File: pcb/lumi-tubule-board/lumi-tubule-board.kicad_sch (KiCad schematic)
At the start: 72 parts, among them Q1 DMN1045UFR4, Q10 DMN1045UFR4, Q11 DMN1045UFR4, Q12 DMN1045UFR4, Q13 DMN1045UFR4, Q2 DMN1045UFR4, Q3 DMN1045UFR4, Q4 DMN1045UFR4, Q5 DMN1045UFR4, Q6 DMN1045UFR4, Q7 DMN1045UFR4, Q8 DMN1045UFR4, Q9 DMN1045UFR4, SW1 SWITCH_TACT_SMT4.6X2.8, SW2 SWITCH_TACT_SMT4.6X2.8, U1 SHTC3, U2 VREG_SOT23-5, U3 ESP32-S3-MINI-1, U4 LIS2Dx12, X1 USB_C

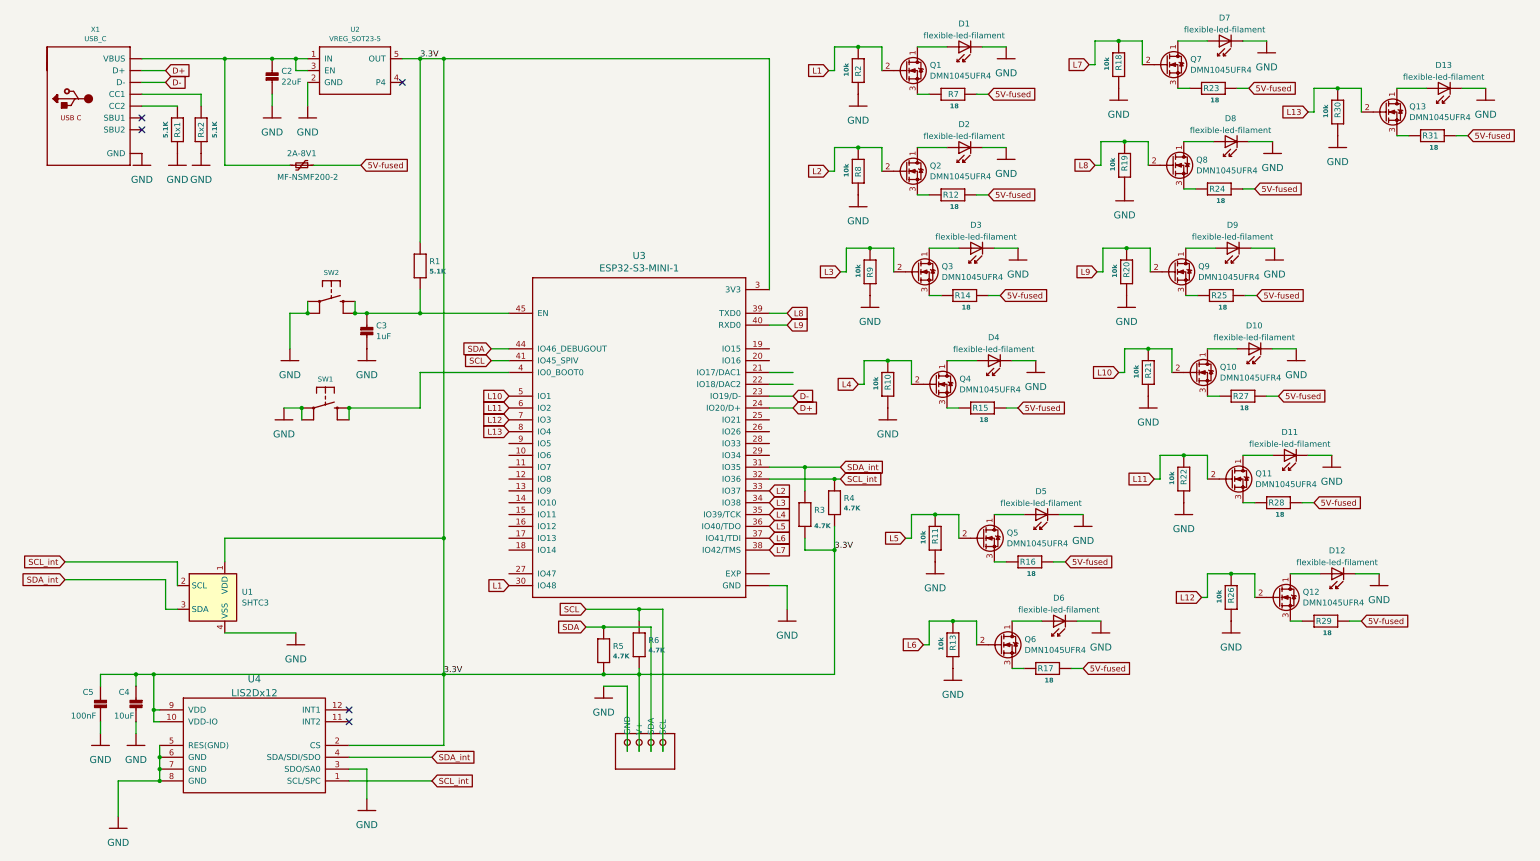
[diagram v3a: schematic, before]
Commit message: Add LED and fix pad numbers
Add low power LED to board and fix some missing links between schematic and pcb design.
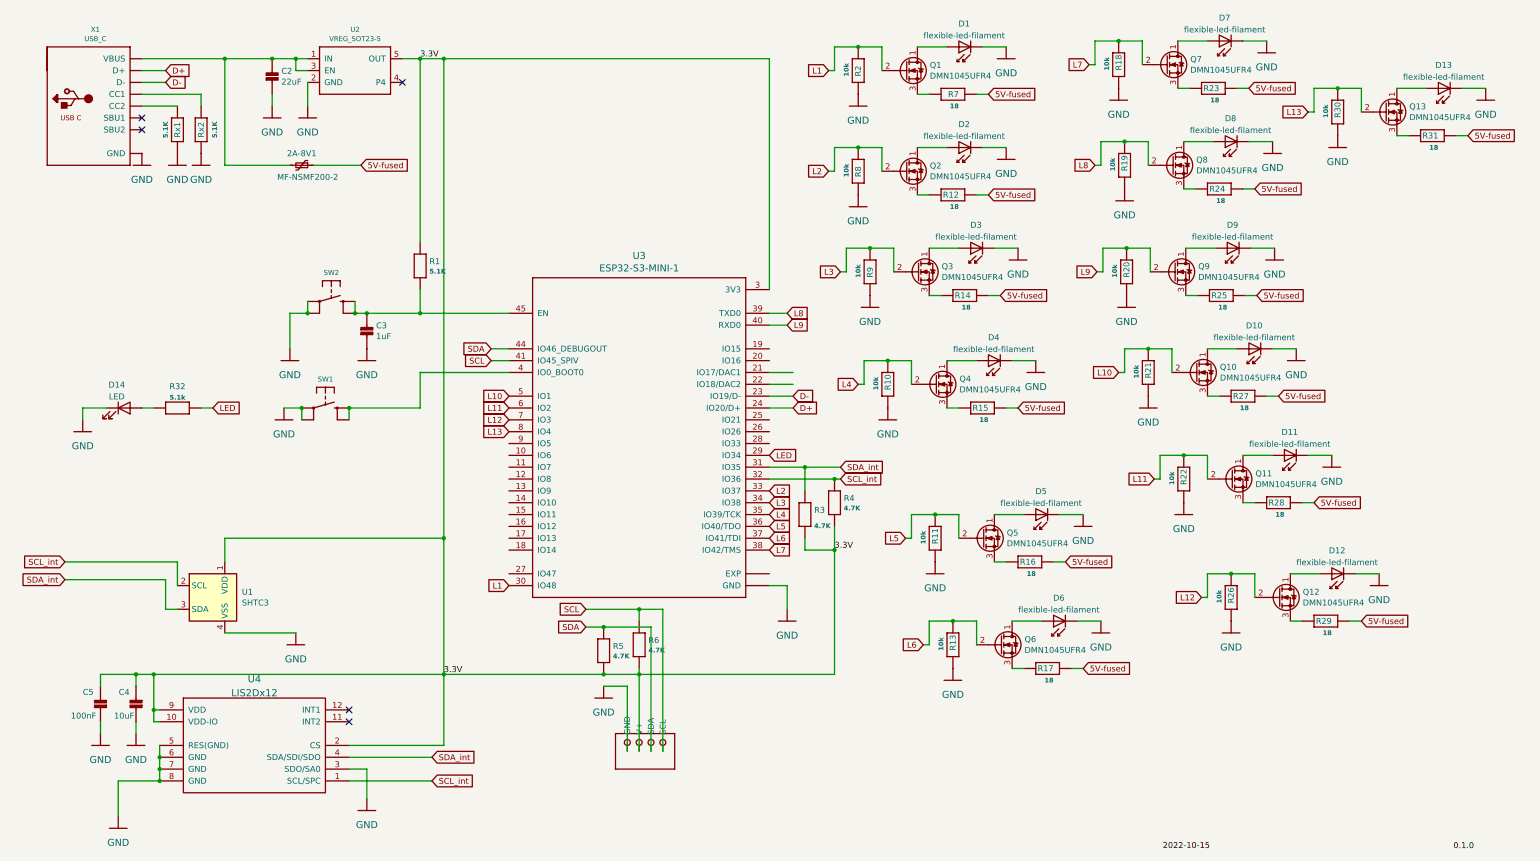
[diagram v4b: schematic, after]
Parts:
- added D14: LED, LED_SMD:LED_0603_1608Metric, symbol Device:LED
- added R32: 5.1k, Resistor_SMD:R_0603_1608Metric, symbol Adafruit_ESP32-S3_8MB_No_PSRAM-eagle-import:RESISTOR_0603
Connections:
- net GND: now also D14.1 (K)
- net LED: now reaches U3.29 (IO34)
- net LED: now also R32.2
- new net: D14.2 (A), R32.1
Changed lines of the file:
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@@
   (no_connect (at 85.09 166.37))
   (no_connect (at 96.52 29.21))
+  (wire (pts (xy 55.88 99.06) (xy 53.34 99.06))
+    (stroke (width 0) (type default) (color 0 0 0 0))
+  )
   (wire (pts (xy 44.45 171.45) (xy 44.45 173.99))
     (stroke (width 0) (type default) (color 0 0 0 0))
@@
     (stroke (width 0) (type default) (color 0 0 0 0))
   )
+  (wire (pts (xy 33.02 99.06) (xy 27.94 99.06))
+    (stroke (width 0) (type default) (color 0 0 0 0))
+  )
   (wire (pts (xy 209.55 149.86) (xy 208.28 149.86))
     (stroke (width 0) (type default) (color 0 0 0 0))
@@
     (stroke (width 0) (type default) (color 0 0 0 0))
   )
+  (wire (pts (xy 27.94 99.06) (xy 27.94 101.6))
+    (stroke (width 0) (type default) (color 0 0 0 0))
+  )
   (wire (pts (xy 195.58 93.98) (xy 194.31 93.98))
     (stroke (width 0) (type default) (color 0 0 0 0))
@@
     (stroke (width 0) (type default) (color 0 0 0 0))
   )
+  (wire (pts (xy 40.64 99.06) (xy 43.18 99.06))
+    (stroke (width 0) (type default) (color 0 0 0 0))
+  )
   (wire (pts (xy 287.02 134.62) (xy 293.37 134.62))
     (stroke (width 0) (type default) (color 0 0 0 0))
@@
     (stroke (width 0) (type default) (color 0 0 0 0))
   )
+  (label "0.1.0" (at 321.9947 193.9738 0)
+    (effects (font (size 1.27 1.27)) (justify left bottom))
+  )
   (label "3.3V" (at 100.33 24.13 0)
     (effects (font (size 1.27 1.27)) (justify left bottom))
@@
     (effects (font (size 1.27 1.27)) (justify left bottom))
   )
+  (label "2022-10-15" (at 259.6468 193.9551 0)
+    (effects (font (size 1.27 1.27)) (justify left bottom))
+  )
   (label "3.3V" (at 189.23 129.54 0)
     (effects (font (size 1.27 1.27)) (justify left bottom))
@@
     )
   )
+  (global_label "LED" (shape input) (at 175.26 109.22 0) (fields_autoplaced)
+    (effects (font (size 1.27 1.27)) (justify left))
+    (property "Intersheet References" "${INTERSHEET_REFS}" (id 0) (at 181.0313 109.1406 0)
+      (effects (font (size 1.27 1.27)) (justify left) hide)
+    )
+  )
   (global_label "5V-fused" (shape input) (at 228.6 99.06 0) (fields_autoplaced)
     (effects (font (size 1.27 1.27)) (justify left))
@@
     )
   )
+  (global_label "LED" (shape input) (at 55.88 99.06 0) (fields_autoplaced)
+    (effects (font (size 1.27 1.27)) (justify left))
+    (property "Intersheet References" "${INTERSHEET_REFS}" (id 0) (at 61.6513 98.9806 0)
+      (effects (font (size 1.27 1.27)) (justify left) hide)
+    )
+  )
   (global_label "L6" (shape input) (at 208.28 149.86 180) (fields_autoplaced)
     (effects (font (size 1.27 1.27)) (justify right))
@@
     (pin "2")
   )
+  (symbol (lib_id "Device:LED") (at 36.83 99.06 0) (unit 1)
+    (in_bom yes) (on_board yes) (fields_autoplaced)
+    (property "Reference" "D14" (id 0) (at 35.2425 94.0902 0))
+    (property "Value" "LED" (id 1) (at 35.2425 96.6271 0))
+    (property "Footprint" "LED_SMD:LED_0603_1608Metric" (id 2) (at 36.83 99.06 0)
+      (effects (font (size 1.27 1.27)) hide)
+    )
+    (property "Datasheet" "https://datasheet.lcsc.com/lcsc/1811101510_Everlight-Elec-19-217-GHC-YR1S2-3T_C72043.pdf" (id 3) (at 36.83 99.06 0)
+      (effects (font (size 1.27 1.27)) hide)
+    )
+    (property "JLCPCB ref" "C72043" (id 4) (at 36.83 99.06 0)
+      (effects (font (size 1.27 1.27)) hide)
+    )
+    (pin "1")
+    (pin "2")
+  )
   (symbol (lib_id "Adafruit_ESP32-S3_8MB_No_PSRAM-eagle-import:GND") (at 281.94 22.86 0) (unit 1)
     (in_bom yes) (on_board yes)
@@
     (pin "1")
   )
+  (symbol (lib_id "Adafruit_ESP32-S3_8MB_No_PSRAM-eagle-import:GND") (at 27.94 104.14 0) (unit 1)
+    (in_bom yes) (on_board yes)
+    (property "Reference" "#GND029" (id 0) (at 27.94 104.14 0)
+      (effects (font (size 1.27 1.27)) hide)
+    )
+    (property "Value" "GND" (id 1) (at 27.94 107.2134 0)
+      (effects (font (size 1.4986 1.4986)))
+    )
+    (property "Footprint" "" (id 2) (at 27.94 104.14 0)
+      (effects (font (size 1.27 1.27)) hide)
+    )
+    (property "Datasheet" "" (id 3) (at 27.94 104.14 0)
+      (effects (font (size 1.27 1.27)) hide)
+    )
+    (pin "1")
+  )
   (symbol (lib_id "Adafruit_ESP32-S3_8MB_No_PSRAM-eagle-import:GND") (at 297.18 43.18 0) (unit 1)
     (in_bom yes) (on_board yes)
@@
     (pin "1")
   )
+  (symbol (lib_id "Adafruit_ESP32-S3_8MB_No_PSRAM-eagle-import:RESISTOR_0603") (at 48.26 99.06 0) (unit 1)
+    (in_bom yes) (on_board yes) (fields_autoplaced)
+    (property "Reference" "R32" (id 0) (at 48.26 94.4294 0))
+    (property "Value" "5.1k" (id 1) (at 48.26 96.7952 0)
+      (effects (font (size 1.016 1.016) bold))
+    )
+    (property "Footprint" "Resistor_SMD:R_0603_1608Metric" (id 2) (at 48.26 99.06 0)
+      (effects (font (size 1.27 1.27)) hide)
+    )
+    (property "Datasheet" "https://datasheet.lcsc.com/lcsc/2206010130_UNI-ROYAL-Uniroyal-Elec-0603WAF2203T5E_C22961.pdf" (id 3) (at 48.26 99.06 0)
+      (effects (font (size 1.27 1.27)) hide)
+    )
+    (property "JLCPCB ref" "C22961" (id 4) (at 48.26 99.06 0)
+      (effects (font (size 1.27 1.27)) hide)
+    )
+    (pin "1")
+    (pin "2")
+  )
   (symbol (lib_id "Adafruit_ESP32-S3_8MB_No_PSRAM-eagle-import:RESISTOR_0603_NOOUT") (at 214.63 149.86 90) (unit 1)
     (in_bom yes) (on_board yes)
@@
       (reference "#GND028") (unit 1) (value "GND") (footprint "")
     )
+    (path "/503ce97c-80b8-42ab-a40d-e82c4bb84960"
+      (reference "#GND029") (unit 1) (value "GND") (footprint "")
+    )
     (path "/00000000-0000-0000-0000-000063154829"
       (reference "#GND0101") (unit 1) (value "GND") (footprint "")
@@
       (reference "D13") (unit 1) (value "flexible-led-filament") (footprint "lumi-tubule-board:Flexible LED filament viamount")
     )
+    (path "/053f1d49-9e2c-4c46-a418-1355f7c965dc"
+      (reference "D14") (unit 1) (value "LED") (footprint "LED_SMD:LED_0603_1608Metric")
+    )
     (path "/00000000-0000-0000-0000-00006318ab1b"
       (reference "Q1") (unit 1) (value "DMN1045UFR4") (footprint "lumi-tubule-board:DMN1045UFR4")
@@
       (reference "R31") (unit 1) (value "18") (footprint "Resistor_SMD:R_1206_3216Metric")
     )
+    (path "/dec5787c-6a1b-4721-bda6-97b2eff8c935"
+      (reference "R32") (unit 1) (value "5.1k") (footprint "Resistor_SMD:R_0603_1608Metric")
+    )
     (path "/00000000-0000-0000-0000-00006317c4f0"

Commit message: Fix MOSFET wiring
Fixed the MOSFETs' wiring, which was all wrong. Rerouted mosfet out via ground plane, freeing up space for the Vsup line on top of board. Removed the diagnosis LED line on the back of PCB which was interrupting ground plane flow. Swapped out the pulldown resistor for something smaller.
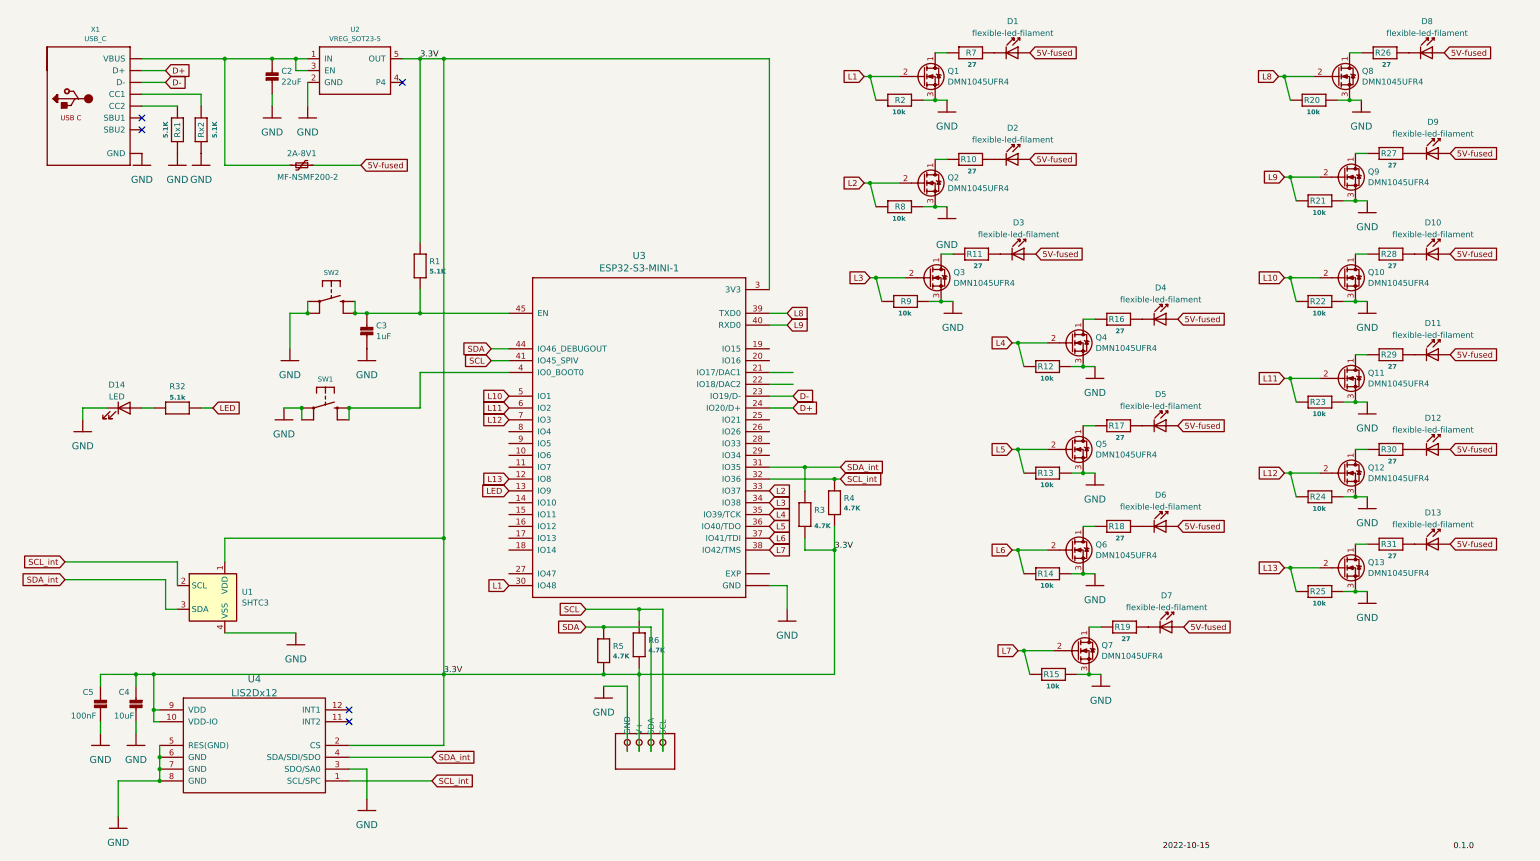
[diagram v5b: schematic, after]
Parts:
- Q1, Q10, Q11, Q12, Q13, Q2, Q3, Q4, Q5, Q6, Q7, Q8, Q9: JLCPCB ref (none) -> C460988
- R10, R11, R18, R19, R26, R30: value 10k -> 27; footprint Resistor_SMD:R_1206_3216Metric -> Resistor_SMD:R_0805_2012Metric; JLCPCB ref (none) -> C966124
- R12, R14, R15, R23, R24, R25: value 18 -> 10k; footprint Resistor_SMD:R_1206_3216Metric -> Resistor_SMD:R_0402_1005Metric; JLCPCB ref (none) -> C25744
- R13, R2, R20, R21, R22, R8, R9: footprint Resistor_SMD:R_1206_3216Metric -> Resistor_SMD:R_0402_1005Metric; JLCPCB ref (none) -> C25744
- R16, R17, R27, R28, R29, R31, R7: value 18 -> 27; footprint Resistor_SMD:R_1206_3216Metric -> Resistor_SMD:R_0805_2012Metric; JLCPCB ref (none) -> C966124
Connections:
- net 5V-fused: now also D1.2 (A), D10.2 (A), D11.2 (A), D12.2 (A), D13.2 (A), D2.2 (A), D3.2 (A), D4.2 (A), D5.2 (A), D6.2 (A), D7.2 (A), D8.2 (A), D9.2 (A); no longer R12.1, R14.1, R15.1, R16.1, R17.1, R23.1, R24.1, R25.1, R27.1, R28.1, R29.1, R31.1, R7.1
- net GND: now also Q1.3 (Source), Q10.3 (Source), Q11.3 (Source), Q12.3 (Source), Q13.3 (Source), Q2.3 (Source), Q3.3 (Source), Q4.3 (Source), Q5.3 (Source), Q6.3 (Source), Q7.3 (Source), Q8.3 (Source), Q9.3 (Source), R12.1, R14.1, R15.1, R23.1, R24.1, R25.1; no longer D1.1 (K), D10.1 (K), D11.1 (K), D12.1 (K), D13.1 (K), D2.1 (K), D3.1 (K), D4.1 (K), D5.1 (K), D6.1 (K), D7.1 (K), D8.1 (K), D9.1 (K), R10.1, R11.1, R18.1, R19.1, R26.1, R30.1
- net L10: now also R22.2; no longer R21.2
- net L11: now also R23.2; no longer R22.2
- net L12: now also R24.2; no longer R26.2
- net L13: now also R25.2, U3.12 (IO8); no longer R30.2, U3.8 (IO4)
- net L4: now also R12.2; no longer R10.2
- net L5: now also R13.2; no longer R11.2
- net L6: now also R14.2; no longer R13.2
- net L7: now also R15.2; no longer R18.2
- net L8: now also R20.2; no longer R19.2
- net L9: now also R21.2; no longer R20.2
- net LED: now also U3.13 (IO9); no longer U3.29 (IO34)
- net at Q1.1 (Drain): now also R7.2; no longer D1.2 (A)
- net at Q13.1 (Drain): now also R31.2; no longer D13.2 (A)
- net at Q4.1 (Drain): now also R16.2; no longer D4.2 (A)
- net at R27.2: now also Q9.1 (Drain); no longer Q10.3 (Source)
- net at Q5.1 (Drain): now also R17.2; no longer D5.2 (A)
- net at Q6.1 (Drain): now also R18.2; no longer D6.2 (A)
- net at Q3.1 (Drain): now also R11.2; no longer D3.2 (A)
- net at Q8.1 (Drain): now also R26.2; no longer D8.2 (A)
- net at Q10.1 (Drain): now also R28.2; no longer D10.2 (A)
- net at Q12.1 (Drain): now also R30.2; no longer D12.2 (A)
- net at R29.2: now also Q11.1 (Drain); no longer Q12.3 (Source)
- net at Q7.1 (Drain): now also R19.2; no longer D7.2 (A)
- net at Q2.1 (Drain): now also R10.2; no longer D2.2 (A)
- new net: D1.1 (K), R7.1
- new net: D10.1 (K), R28.1
- new net: D11.1 (K), R29.1
- new net: D2.1 (K), R10.1
- new net: D3.1 (K), R11.1
- new net: D12.1 (K), R30.1
- new net: D8.1 (K), R26.1
- new net: D4.1 (K), R16.1
- new net: D7.1 (K), R19.1
- new net: D13.1 (K), R31.1
- new net: D9.1 (K), R27.1
- new net: D6.1 (K), R18.1
- new net: D5.1 (K), R17.1
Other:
- moved on the sheet: D1, Q1, R2, R7
